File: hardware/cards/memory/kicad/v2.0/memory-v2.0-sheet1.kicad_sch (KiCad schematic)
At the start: 29 parts, among them IC12 74*74, IC3 74*32, X1 FABC96R

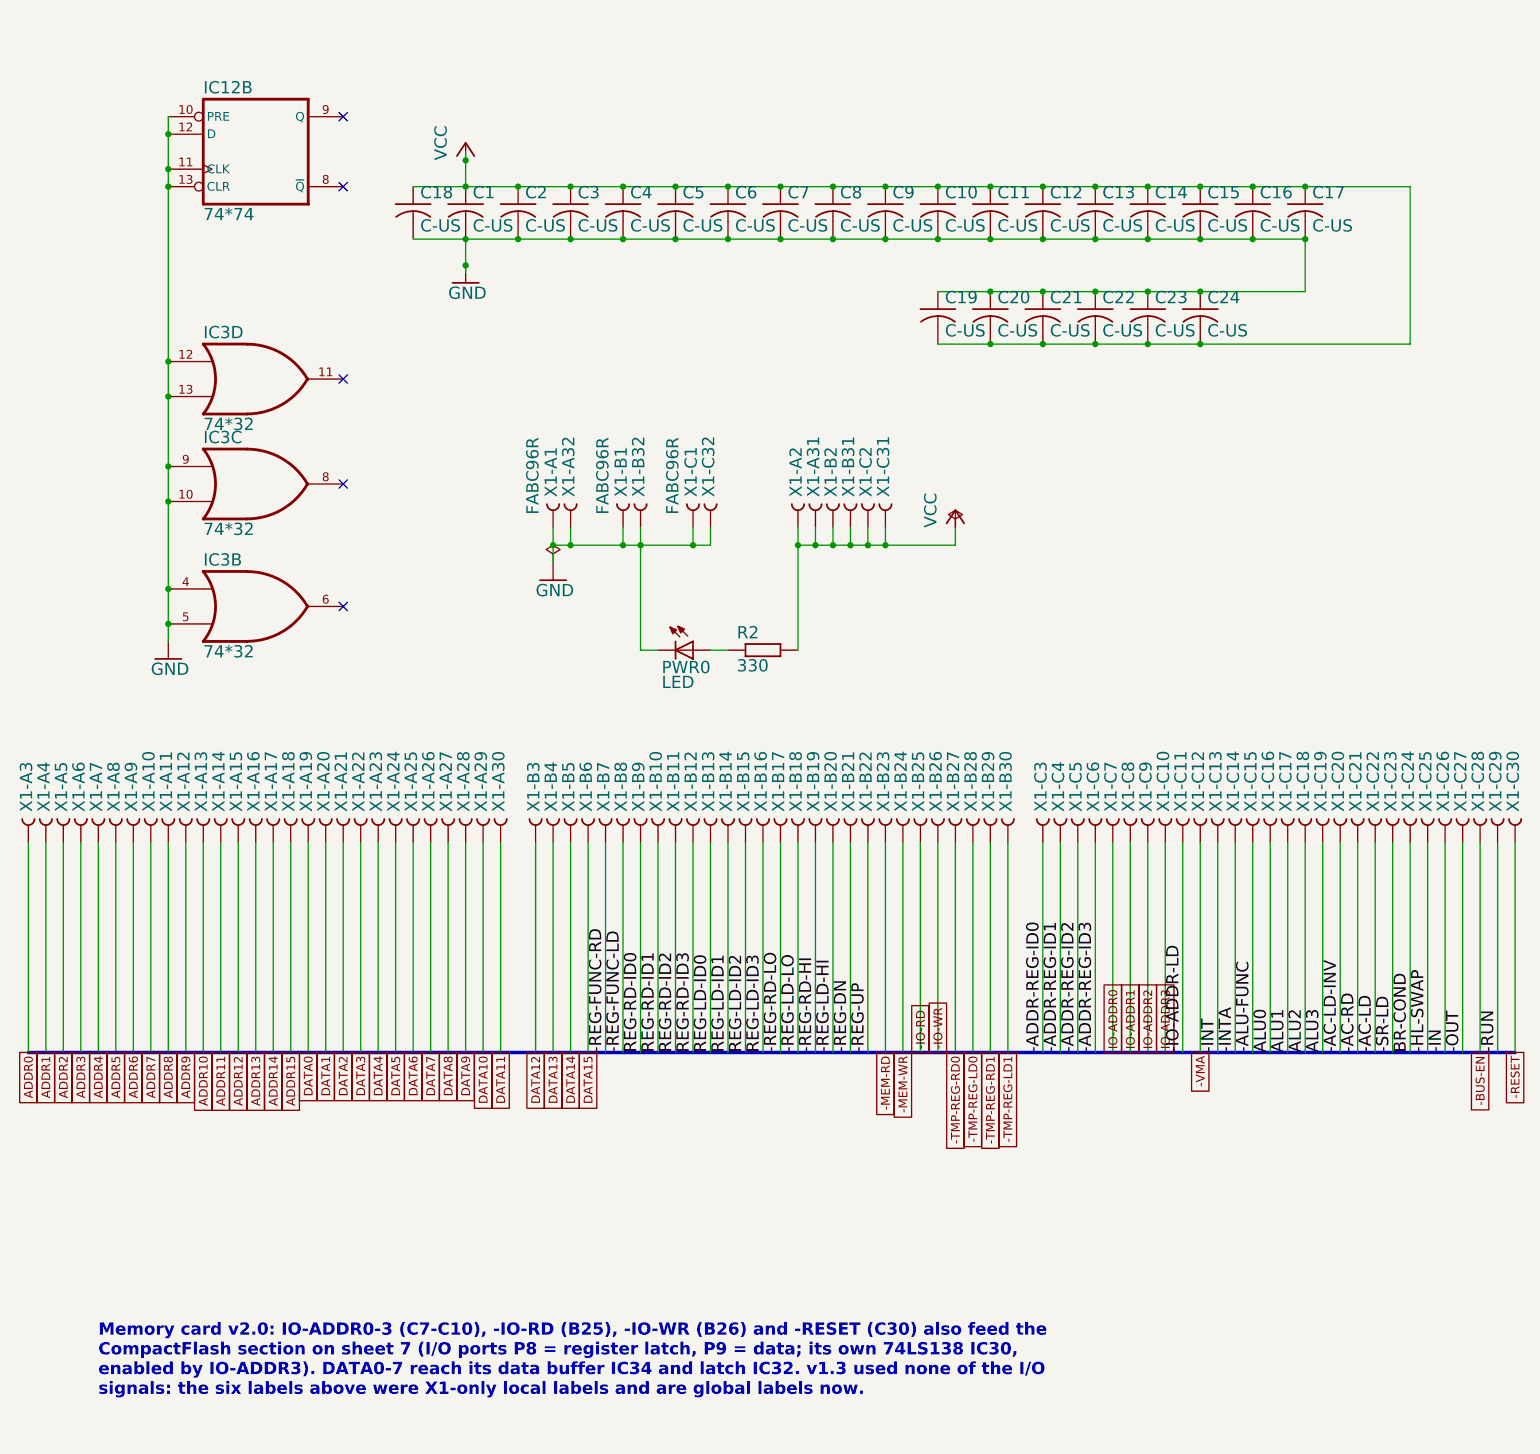
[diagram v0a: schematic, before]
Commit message: feat(memory): rebuild memory card v2.0 on the built card - CF section does not fit, placement blocked
hardware/cards/memory/kicad/v2.0 is now generated from ../v1.3-fusion-export-2026-09-24 (the built
card) instead of the earlier save: v2.0 = built card + the CF section (CF card v1.0 circuit on P8/P9,
IC30-IC34, J2/J3/JP2, RN9, R10-R14, LED1, C25-C30), IC15 included with its real wiring. Netlist proof
MATCH pin for pin (74 parts, 186 nets; every option board = the schematic); ERC 99 = the built
card's 104 + SRST - the six labels made global.

The built card's copper is locked: gen_mem_v2.py no longer trims or drops copper, it refuses moves
that would break a track, and "locked" proves all 1377 track segments/vias present unchanged on
every board. FAB_MOVES and the reserved IC15 spot are gone (the parts are simply the built card's).
The built card's Eagle rules that are stricter than the project's go into memory-v2.0.kicad_dru
(18 mil track-track, 10 mil track-pad). build.sh now gates on the summary files (a pipeline hid
failed gates before).

Result: the built card routes DATA8-15 to the TMP registers as a bundle across the lower right of
the board, through the slots the three options used. Every option has CF pads on built tracks
(A 11 shorts / 4 clearance / 63 mask bridges, B 12/1/50, C 12/3/63). space_check.py shows no legal
placement exists: at most 4 of the 5 CF DIPs fit even with no IDE header and none of the other 16
CF parts (2 with J2 where option C puts it). Not routed, not ordered; README lists the ways forward
(re-route that bundle, keep the separate CF card, SMD CF logic, or a new layout). Docs and BACKLOG
say v2.0 is blocked.

Co-Authored-By: Claude Opus 5.5 <noreply@anthropic.com>
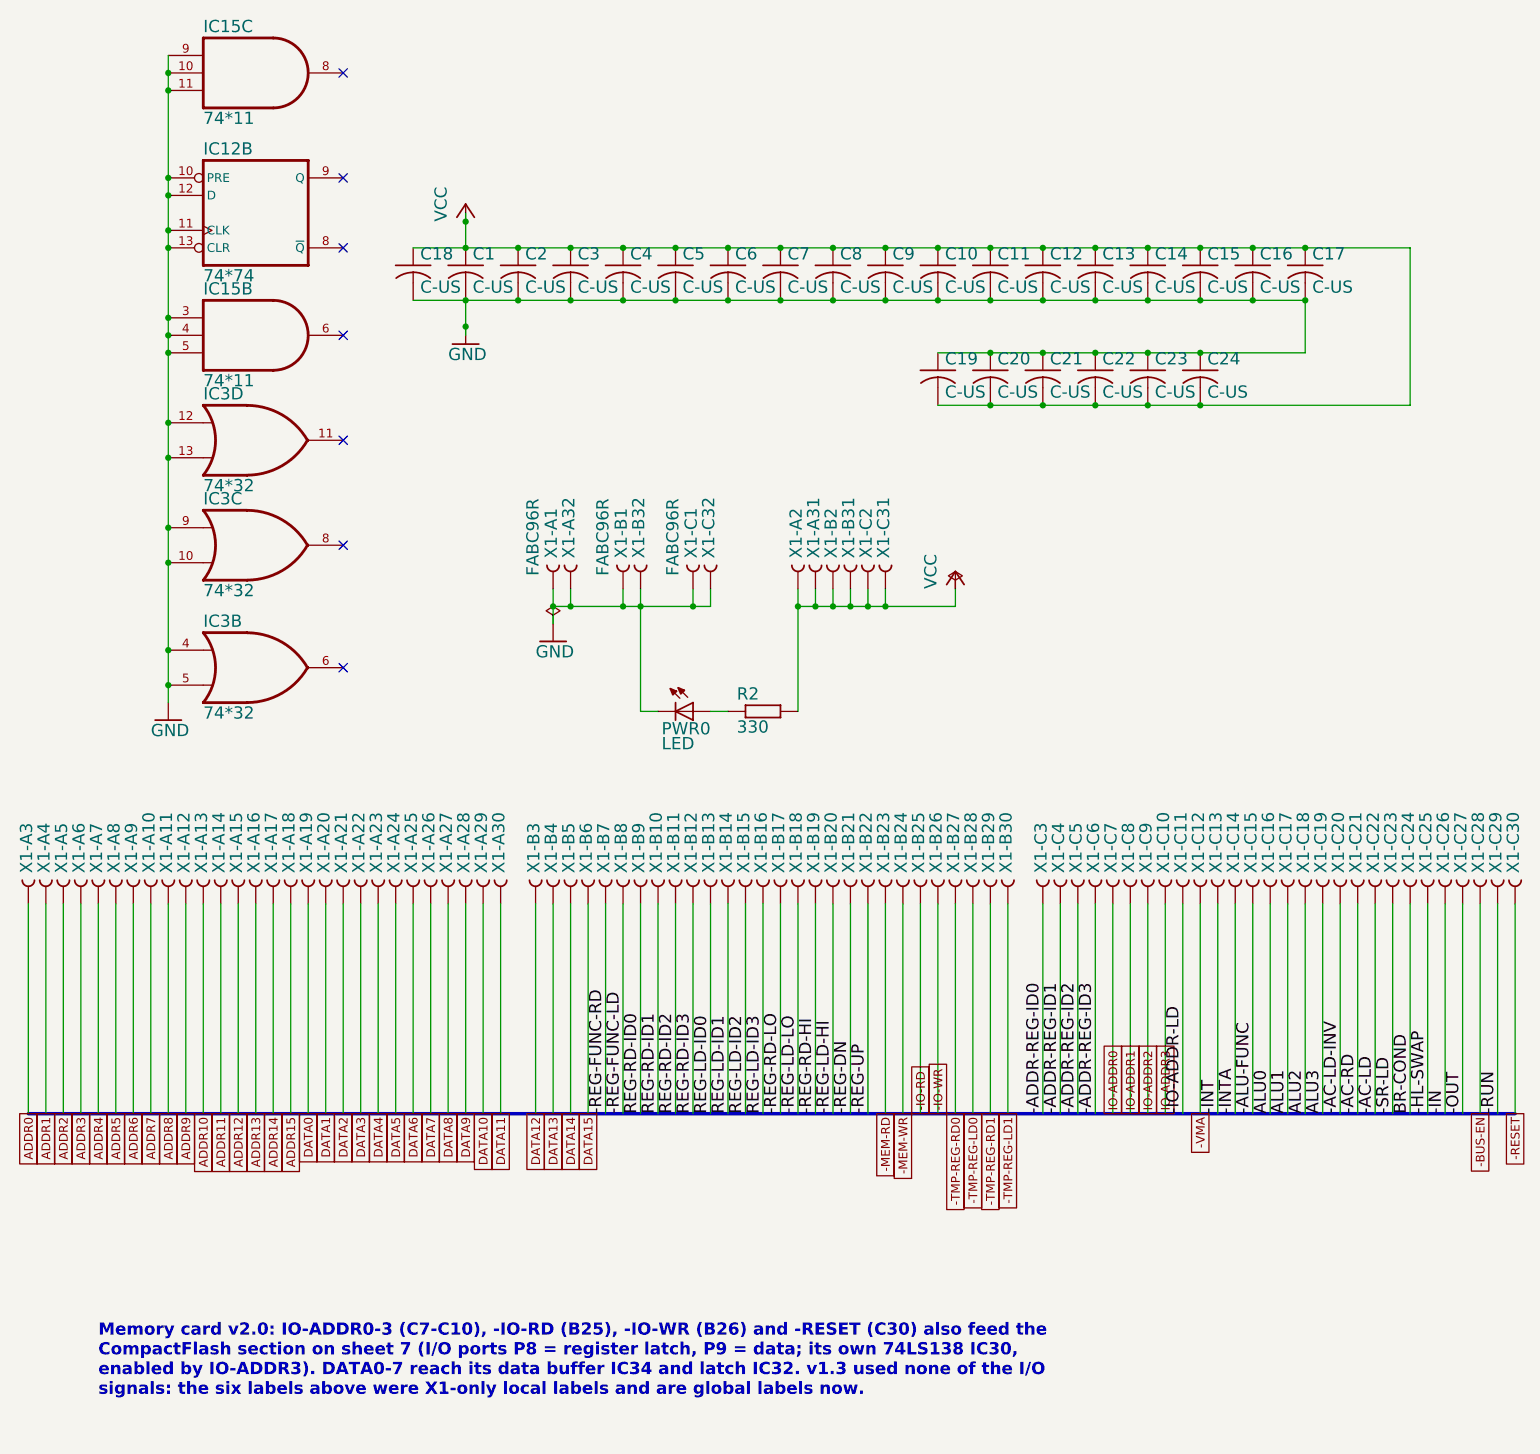
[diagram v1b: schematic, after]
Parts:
- removed C1, C10, C11, C12, C13, C14, C15, C16, C17, C18, C19, C2, C20, C21, C22, C23, C24, C3, C4, C5, C6, C7, C8, C9: C-US, memory-v1.3-eagle:C025-025X050, symbol memory-v1.3-eagle:adafruit_C-US_025-025X050
- removed IC12: 74*74, memory-v1.3-eagle:DIL14, symbol memory-v1.3-eagle:74xx-us_74x74_N_pwrhidden
- removed IC3: 74*32, memory-v1.3-eagle:DIL14, symbol memory-v1.3-eagle:74xx-us_74x32_N_pwrhidden
- removed PWR0: LED, memory-v1.3-eagle:LED5MM, symbol memory-v1.3-eagle:led_LED_5MM
- removed R2: 330, memory-v1.3-eagle:0207_10, symbol memory-v1.3-eagle:eagle-ltspice_R_0207_10
- removed X1: FABC96R, memory-v1.3-eagle:FABC96R, symbol memory-v1.3-eagle:con-vg_FABC96R
- added C1, C10, C11, C12, C13, C14, C15, C16, C17, C18, C19, C2, C20, C21, C22, C23, C24, C3, C4, C5, C6, C7, C8, C9: C-US, memory-v1.3-fusion-export-2026-09-24-eagle:C025-025X050, symbol memory-v1.3-fusion-export-2026-09-24-eagle:adafruit_C-US_025-025X050
- added IC12: 74*74, memory-v1.3-fusion-export-2026-09-24-eagle:DIL14, symbol memory-v1.3-fusion-export-2026-09-24-eagle:74xx-us_74x74_N_pwrhidden
- added IC15: 74*11, memory-v1.3-fusion-export-2026-09-24-eagle:DIL14, symbol memory-v1.3-fusion-export-2026-09-24-eagle:74xx-us_74x11_N_pwrhidden
- added IC3: 74*32, memory-v1.3-fusion-export-2026-09-24-eagle:DIL14, symbol memory-v1.3-fusion-export-2026-09-24-eagle:74xx-us_74x32_N_pwrhidden
- added PWR0: LED, memory-v1.3-fusion-export-2026-09-24-eagle:LED5MM, symbol memory-v1.3-fusion-export-2026-09-24-eagle:led_LED_5MM
- added R2: 330, memory-v1.3-fusion-export-2026-09-24-eagle:0207_10, symbol memory-v1.3-fusion-export-2026-09-24-eagle:eagle-ltspice_R_0207_10
- added X1: FABC96R, memory-v1.3-fusion-export-2026-09-24-eagle:FABC96R, symbol memory-v1.3-fusion-export-2026-09-24-eagle:con-vg_FABC96R
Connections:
- net -AC-LD: now also X1.C22 (B)
- net -AC-LD-INV: now also X1.C20 (B)
- net -AC-RD: now also X1.C21 (B)
- net -ADDR-REG-ID0: now also X1.C3 (B)
- net -ADDR-REG-ID1: now also X1.C4 (B)
- net -ADDR-REG-ID2: now also X1.C5 (B)
- net -ADDR-REG-ID3: now also X1.C6 (B)
- net -ALU-FUNC: now also X1.C15 (B)
- net -BUS-EN: now also X1.C28 (B)
- net -HL-SWAP: now also X1.C25 (B)
- net -IN: now also X1.C26 (B)
- net -INT: now also X1.C13 (B)
- net -INTA: now also X1.C14 (B)
- net -IO-ADDR-LD: now also X1.C11 (B)
- net -IO-RD: now also X1.B25 (B)
- net -IO-WR: now also X1.B26 (B)
- net -MEM-RD: now also X1.B23 (B)
- net -MEM-WR: now also X1.B24 (B)
- net -OUT: now also X1.C27 (B)
- net -REG-DN: now also X1.B21 (B)
- net -REG-FUNC-LD: now also X1.B8 (B)
- net -REG-FUNC-RD: now also X1.B7 (B)
- net -REG-LD-HI: now also X1.B20 (B)
- net -REG-LD-LO: now also X1.B18 (B)
- net -REG-RD-HI: now also X1.B19 (B)
- net -REG-RD-LO: now also X1.B17 (B)
- net -REG-UP: now also X1.B22 (B)
- net -RESET: now also X1.C30 (B)
- net -RUN: now also X1.C29 (B)
- net -SR-LD: now also X1.C23 (B)
- net -TMP-REG-LD0: now also X1.B28 (B)
- net -TMP-REG-LD1: now also X1.B30 (B)
- net -TMP-REG-RD0: now also X1.B27 (B)
- net -TMP-REG-RD1: now also X1.B29 (B)
- net -VMA: now also X1.C12 (B)
- net ADDR0: now also X1.A3 (B)
- net ADDR1: now also X1.A4 (B)
- net ADDR10: now also X1.A13 (B)
- net ADDR11: now also X1.A14 (B)
- net ADDR12: now also X1.A15 (B)
- net ADDR13: now also X1.A16 (B)
- net ADDR14: now also X1.A17 (B)
- net ADDR15: now also X1.A18 (B)
- net ADDR2: now also X1.A5 (B)
- net ADDR3: now also X1.A6 (B)
- net ADDR4: now also X1.A7 (B)
- net ADDR5: now also X1.A8 (B)
- net ADDR6: now also X1.A9 (B)
- net ADDR7: now also X1.A10 (B)
- net ADDR8: now also X1.A11 (B)
- net ADDR9: now also X1.A12 (B)
- net ALU0: now also X1.C16 (B)
- net ALU1: now also X1.C17 (B)
- net ALU2: now also X1.C18 (B)
- net ALU3: now also X1.C19 (B)
- net BR-COND: now also X1.C24 (B)
- net DATA0: now also X1.A19 (B)
- net DATA1: now also X1.A20 (B)
- net DATA10: now also X1.A29 (B)
- net DATA11: now also X1.A30 (B)
- net DATA12: now also X1.B3 (B)
- net DATA13: now also X1.B4 (B)
- net DATA14: now also X1.B5 (B)
- net DATA15: now also X1.B6 (B)
- net DATA2: now also X1.A21 (B)
- net DATA3: now also X1.A22 (B)
- net DATA4: now also X1.A23 (B)
- net DATA5: now also X1.A24 (B)
- net DATA6: now also X1.A25 (B)
- net DATA7: now also X1.A26 (B)
- net DATA8: now also X1.A27 (B)
- net DATA9: now also X1.A28 (B)
- net GND: now also C1.2, C10.2, C11.2, C12.2, C13.2, C14.2, C15.2, C16.2, C17.2, C18.2, C19.1, C2.2, C20.1, C21.1, C22.1, C23.1, C24.1, C3.2, C4.2, C5.2, C6.2, C7.2, C8.2, C9.2, IC12.10 (PRE), IC12.11 (CLK), IC12.12 (D), IC12.13 (CLR), IC12.7 (GND), IC15.10 (I1), IC15.11 (I2), IC15.3 (I0), IC15.4 (I1), IC15.5 (I2), IC15.7 (GND), IC15.7 (GND), IC15.9 (I0), IC3.10 (I1), IC3.12 (I0), IC3.13 (I1), IC3.4 (I0), IC3.5 (I1), IC3.7 (GND), IC3.7 (GND), IC3.7 (GND), IC3.9 (I0), PWR0.K (C), X1.A1 (B), X1.A32 (B), X1.B1 (B), X1.B32 (B), X1.C1 (B), X1.C32 (B)
- net IO-ADDR0: now also X1.C7 (B)
- net IO-ADDR1: now also X1.C8 (B)
- net IO-ADDR2: now also X1.C9 (B)
- net IO-ADDR3: now also X1.C10 (B)
- net REG-LD-ID0: now also X1.B13 (B)
- net REG-LD-ID1: now also X1.B14 (B)
- net REG-LD-ID2: now also X1.B15 (B)
- net REG-LD-ID3: now also X1.B16 (B)
- net REG-RD-ID0: now also X1.B9 (B)
- net REG-RD-ID1: now also X1.B10 (B)
- net REG-RD-ID2: now also X1.B11 (B)
- net REG-RD-ID3: now also X1.B12 (B)
- net VCC: now also C1.1, C10.1, C11.1, C12.1, C13.1, C14.1, C15.1, C16.1, C17.1, C18.1, C19.2, C2.1, C20.2, C21.2, C22.2, C23.2, C24.2, C3.1, C4.1, C5.1, C6.1, C7.1, C8.1, C9.1, IC12.14 (VCC), IC15.14 (VCC), IC15.14 (VCC), IC3.14 (VCC), IC3.14 (VCC), IC3.14 (VCC), R2.2, X1.A2 (B), X1.A31 (B), X1.B2 (B), X1.B31 (B), X1.C2 (B), X1.C31 (B)
- new net: PWR0.A, R2.1
- no-connect marks 5 -> 7

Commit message: refactor(memory): built card is eagle/v1.3; the earlier save is eagle/deprecated/v1.3-do-not-use
Ken 2026-09-24: the memory card folders are renamed so the plain v1.3 name is the card in the machine.

- eagle/v1.3/ (earlier save, notes 2025-03-06, board 2021-03-17, NOT the built card) -> eagle/deprecated/v1.3-do-not-use/
  (git mv, contents untouched); its KiCad conversion regenerated as kicad/deprecated/v1.3-do-not-use/ (project
  memory-v1.3-do-not-use, proof MATCH 115/115, still "never fabricated").
- eagle/v1.3-fusion-export-2026-09-24/ (the BUILT card: Ken's Fusion 360 export of 2026-09-24, verified against JLCPCB
  order 2000765A) -> eagle/v1.3/; its conversion regenerated as kicad/v1.3/ (memory-v1.3.*, proof MATCH 116/116).
  verify_fab_vs_brd.py: PASS on eagle/v1.3 (all 695 holes, 1,263 tracks, parts, PnP; gerber set byte-identical to
  the one kept in the deprecated folder), FAIL on the deprecated board as before.
- Migration plan: tools/migrate_dryrun.py sends GV "Memory v1.3" to eagle/deprecated/v1.3-do-not-use/; migration/
  reports re-run (the 30 plan rows differ only by that destination). audit_tree.py: the Fusion-export rule now
  matches eagle/v1.3/ and is checked before the 2026-09-20 run log (which lists the earlier save at that path).
  Audit: 0 unexplained, 0 hash mismatches, 0 plan rows missing.
- fabricated.py -> FABRICATED.md + marker, gen_bom.py (+ docs/bom rows, --check up to date), PROVENANCE.md
  regenerated, KICAD.md rows (stale fusion-export row removed), BOARDS.md/SCHEMATICS.md rows, the memory section of
  DESIGN-REVIEW.md (now the built card: 53 parts, 169 nets, 21 ICs; the rest of that file is left at its 09-21 run).
- memory v2.0 reads ../v1.3: BASE_NAME/BASE/space_check path/docstrings/MASTER/README. The copied library is renamed
  memory-v1.3-eagle (the regenerated base's nickname; gen_mem_v2.py sch copies it with the lib tables). The converter
  derives schematic UUIDs from the project name, so in the boards a NOROUTE build does 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
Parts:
- removed C1, C10, C11, C12, C13, C14, C15, C16, C17, C18, C19, C2, C20, C21, C22, C23, C24, C3, C4, C5, C6, C7, C8, C9: C-US, memory-v1.3-fusion-export-2026-09-24-eagle:C025-025X050, symbol memory-v1.3-fusion-export-2026-09-24-eagle:adafruit_C-US_025-025X050
- removed IC12: 74*74, memory-v1.3-fusion-export-2026-09-24-eagle:DIL14, symbol memory-v1.3-fusion-export-2026-09-24-eagle:74xx-us_74x74_N_pwrhidden
- removed IC15: 74*11, memory-v1.3-fusion-export-2026-09-24-eagle:DIL14, symbol memory-v1.3-fusion-export-2026-09-24-eagle:74xx-us_74x11_N_pwrhidden
- removed IC3: 74*32, memory-v1.3-fusion-export-2026-09-24-eagle:DIL14, symbol memory-v1.3-fusion-export-2026-09-24-eagle:74xx-us_74x32_N_pwrhidden
- removed PWR0: LED, memory-v1.3-fusion-export-2026-09-24-eagle:LED5MM, symbol memory-v1.3-fusion-export-2026-09-24-eagle:led_LED_5MM
- removed R2: 330, memory-v1.3-fusion-export-2026-09-24-eagle:0207_10, symbol memory-v1.3-fusion-export-2026-09-24-eagle:eagle-ltspice_R_0207_10
- removed X1: FABC96R, memory-v1.3-fusion-export-2026-09-24-eagle:FABC96R, symbol memory-v1.3-fusion-export-2026-09-24-eagle:con-vg_FABC96R
- added C1, C10, C11, C12, C13, C14, C15, C16, C17, C18, C19, C2, C20, C21, C22, C23, C24, C3, C4, C5, C6, C7, C8, C9: C-US, memory-v1.3-eagle:C025-025X050, symbol memory-v1.3-eagle:adafruit_C-US_025-025X050
- added IC12: 74*74, memory-v1.3-eagle:DIL14, symbol memory-v1.3-eagle:74xx-us_74x74_N_pwrhidden
- added IC15: 74*11, memory-v1.3-eagle:DIL14, symbol memory-v1.3-eagle:74xx-us_74x11_N_pwrhidden
- added IC3: 74*32, memory-v1.3-eagle:DIL14, symbol memory-v1.3-eagle:74xx-us_74x32_N_pwrhidden
- added PWR0: LED, memory-v1.3-eagle:LED5MM, symbol memory-v1.3-eagle:led_LED_5MM
- added R2: 330, memory-v1.3-eagle:0207_10, symbol memory-v1.3-eagle:eagle-ltspice_R_0207_10
- added X1: FABC96R, memory-v1.3-eagle:FABC96R, symbol memory-v1.3-eagle:con-vg_FABC96R
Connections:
- net -AC-LD: now also X1.C22 (B)
- net -AC-LD-INV: now also X1.C20 (B)
- net -AC-RD: now also X1.C21 (B)
- net -ADDR-REG-ID0: now also X1.C3 (B)
- net -ADDR-REG-ID1: now also X1.C4 (B)
- net -ADDR-REG-ID2: now also X1.C5 (B)
- net -ADDR-REG-ID3: now also X1.C6 (B)
- net -ALU-FUNC: now also X1.C15 (B)
- net -BUS-EN: now also X1.C28 (B)
- net -HL-SWAP: now also X1.C25 (B)
- net -IN: now also X1.C26 (B)
- net -INT: now also X1.C13 (B)
- net -INTA: now also X1.C14 (B)
- net -IO-ADDR-LD: now also X1.C11 (B)
- net -IO-RD: now also X1.B25 (B)
- net -IO-WR: now also X1.B26 (B)
- net -MEM-RD: now also X1.B23 (B)
- net -MEM-WR: now also X1.B24 (B)
- net -OUT: now also X1.C27 (B)
- net -REG-DN: now also X1.B21 (B)
- net -REG-FUNC-LD: now also X1.B8 (B)
- net -REG-FUNC-RD: now also X1.B7 (B)
- net -REG-LD-HI: now also X1.B20 (B)
- net -REG-LD-LO: now also X1.B18 (B)
- net -REG-RD-HI: now also X1.B19 (B)
- net -REG-RD-LO: now also X1.B17 (B)
- net -REG-UP: now also X1.B22 (B)
- net -RESET: now also X1.C30 (B)
- net -RUN: now also X1.C29 (B)
- net -SR-LD: now also X1.C23 (B)
- net -TMP-REG-LD0: now also X1.B28 (B)
- net -TMP-REG-LD1: now also X1.B30 (B)
- net -TMP-REG-RD0: now also X1.B27 (B)
- net -TMP-REG-RD1: now also X1.B29 (B)
- net -VMA: now also X1.C12 (B)
- net ADDR0: now also X1.A3 (B)
- net ADDR1: now also X1.A4 (B)
- net ADDR10: now also X1.A13 (B)
- net ADDR11: now also X1.A14 (B)
- net ADDR12: now also X1.A15 (B)
- net ADDR13: now also X1.A16 (B)
- net ADDR14: now also X1.A17 (B)
- net ADDR15: now also X1.A18 (B)
- net ADDR2: now also X1.A5 (B)
- net ADDR3: now also X1.A6 (B)
- net ADDR4: now also X1.A7 (B)
- net ADDR5: now also X1.A8 (B)
- net ADDR6: now also X1.A9 (B)
- net ADDR7: now also X1.A10 (B)
- net ADDR8: now also X1.A11 (B)
- net ADDR9: now also X1.A12 (B)
- net ALU0: now also X1.C16 (B)
- net ALU1: now also X1.C17 (B)
- net ALU2: now also X1.C18 (B)
- net ALU3: now also X1.C19 (B)
- net BR-COND: now also X1.C24 (B)
- net DATA0: now also X1.A19 (B)
- net DATA1: now also X1.A20 (B)
- net DATA10: now also X1.A29 (B)
- net DATA11: now also X1.A30 (B)
- net DATA12: now also X1.B3 (B)
- net DATA13: now also X1.B4 (B)
- net DATA14: now also X1.B5 (B)
- net DATA15: now also X1.B6 (B)
- net DATA2: now also X1.A21 (B)
- net DATA3: now also X1.A22 (B)
- net DATA4: now also X1.A23 (B)
- net DATA5: now also X1.A24 (B)
- net DATA6: now also X1.A25 (B)
- net DATA7: now also X1.A26 (B)
- net DATA8: now also X1.A27 (B)
- net DATA9: now also X1.A28 (B)
- net GND: now also C1.2, C10.2, C11.2, C12.2, C13.2, C14.2, C15.2, C16.2, C17.2, C18.2, C19.1, C2.2, C20.1, C21.1, C22.1, C23.1, C24.1, C3.2, C4.2, C5.2, C6.2, C7.2, C8.2, C9.2, IC12.10 (PRE), IC12.11 (CLK), IC12.12 (D), IC12.13 (CLR), IC12.7 (GND), IC15.10 (I1), IC15.11 (I2), IC15.3 (I0), IC15.4 (I1), IC15.5 (I2), IC15.7 (GND), IC15.7 (GND), IC15.9 (I0), IC3.10 (I1), IC3.12 (I0), IC3.13 (I1), IC3.4 (I0), IC3.5 (I1), IC3.7 (GND), IC3.7 (GND), IC3.7 (GND), IC3.9 (I0), PWR0.K (C), X1.A1 (B), X1.A32 (B), X1.B1 (B), X1.B32 (B), X1.C1 (B), X1.C32 (B)
- net IO-ADDR0: now also X1.C7 (B)
- net IO-ADDR1: now also X1.C8 (B)
- net IO-ADDR2: now also X1.C9 (B)
- net IO-ADDR3: now also X1.C10 (B)
- net REG-LD-ID0: now also X1.B13 (B)
- net REG-LD-ID1: now also X1.B14 (B)
- net REG-LD-ID2: now also X1.B15 (B)
- net REG-LD-ID3: now also X1.B16 (B)
- net REG-RD-ID0: now also X1.B9 (B)
- net REG-RD-ID1: now also X1.B10 (B)
- net REG-RD-ID2: now also X1.B11 (B)
- net REG-RD-ID3: now also X1.B12 (B)
- net VCC: now also C1.1, C10.1, C11.1, C12.1, C13.1, C14.1, C15.1, C16.1, C17.1, C18.1, C19.2, C2.1, C20.2, C21.2, C22.2, C23.2, C24.2, C3.1, C4.1, C5.1, C6.1, C7.1, C8.1, C9.1, IC12.14 (VCC), IC15.14 (VCC), IC15.14 (VCC), IC3.14 (VCC), IC3.14 (VCC), IC3.14 (VCC), R2.2, X1.A2 (B), X1.A31 (B), X1.B2 (B), X1.B31 (B), X1.C2 (B), X1.C31 (B)
- new net: PWR0.A, R2.1
